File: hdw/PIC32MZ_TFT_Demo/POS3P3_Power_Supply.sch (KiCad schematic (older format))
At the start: 12 parts, among them U401 TPS62150

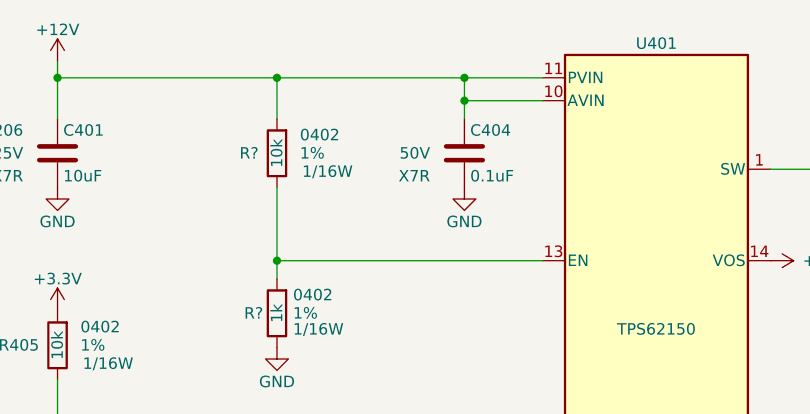
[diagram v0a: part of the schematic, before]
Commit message: Added TFT screen sch sheet
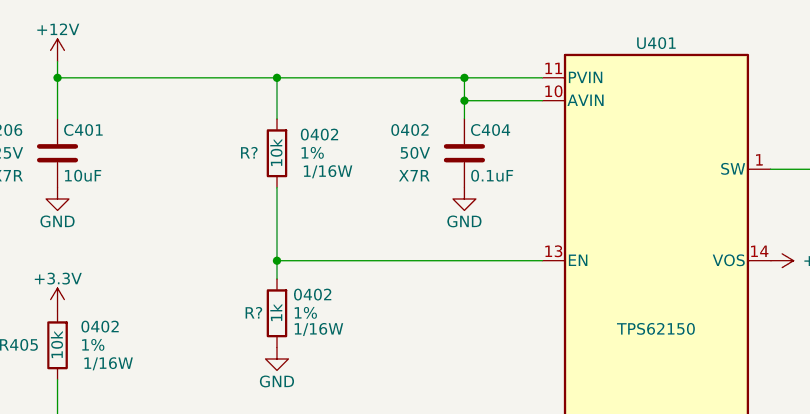
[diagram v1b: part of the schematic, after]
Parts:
- C404: display_footprint (none) -> 0402
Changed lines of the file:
@@
 F 2 "Capacitors_SMD:C_0402" H 4588 2820 50  0001 C CNN
 F 3 "" H 4575 3070 50  0001 C CNN
-F 4 "" H 4400 3070 50  0000 R CNN "display_footprint"
+F 4 "0402" H 4400 3070 50  0000 R CNN "display_footprint"
 F 5 "50V" H 4400 2970 50  0000 R CNN "Voltage"
 F 6 "X7R" H 4400 2870 50  0000 R CNN "Dielectric"

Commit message: Started PCB layout
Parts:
- gave numbers to parts that had none: 2
- renumbered C401 to C301, C403 to C302, C404 to C303, C405 to C304, L401 to L301, R405 to R301, R410 to R304, R411 to R305, TP401 to TP301, U401 to U301
